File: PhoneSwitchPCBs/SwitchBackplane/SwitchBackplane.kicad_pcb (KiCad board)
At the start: 2 copper layers, 255 parts, among them J1 Power, J10 Trunk 1, J11 Trunk 2, J12 UART, J13 SWD, J2 Station 1, J3 Station 2, J4 Station 3, J5 Station 4, J6 Station 5, J7 Station 6, J8 Station 7, J9 Station 8, Q1 XP231N02013R-G, Q10 XP231N02013R-G, Q11 XP231N02013R-G, Q12 PMV65XP, Q2 XP231N02013R-G, Q3 XP231N02013R-G, Q4 XP231N02013R-G, Q5 XP231N02013R-G, Q6 XP231N02013R-G, Q7 XP231N02013R-G, Q8 XP231N02013R-G, Q9 XP231N02013R-G, T1 FS28-200-C2, U1 Pi Pico, U10 XRA1403IG24TR-F, U11 TL071, U12 TL071, U13 XRA1403IG24TR-F, U14 XRA1403IG24TR-F, U15 XRA1403IG24TR-F, U2 TL074, U3 TL074, U4 74HC4316, U5 TL071, U6 MT8870DS1, U7 TPA3144D2PWPR, U8 MT8870DS1, U9 74HC4316, Y1 3.579545 MHz

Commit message: More work on PCB
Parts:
- added H1: GND, MountingHole:MountingHole_3.2mm_M3_Pad, F.Cu at (53.5, 60.8)
- added H2: GND, MountingHole:MountingHole_3.2mm_M3_Pad, F.Cu at (53.5, 155.1)
- added H3: GND, MountingHole:MountingHole_3.2mm_M3_Pad, F.Cu at (221.2, 60.8)
- added H4: GND, MountingHole:MountingHole_3.2mm_M3_Pad, F.Cu at (221.2, 155.1)
- added H5: GND, MountingHole:MountingHole_3.2mm_M3_Pad, F.Cu at (389.0, 60.8)
- added H6: GND, MountingHole:MountingHole_3.2mm_M3_Pad, F.Cu at (389.0, 155.1)
- moved C3 139.3 mm to (266.8, 227.1)
- moved C38 139.3 mm to (190.7, 256.9)
- moved Q7 139.3 mm to (210.1, 256.9)
- moved R52 139.3 mm to (266.8, 229.6)
- moved R91 139.3 mm to (266.8, 224.6)
- moved U3 139.3 mm to (264.8, 179.9)
- moved C1 139.3 mm to (145.2, 260.1)
- moved C10 139.3 mm to (233.4, 234.7)
- moved C11 139.3 mm to (266.7, 232.1)
- moved C12 139.3 mm to (281.5, 215.8)
- moved C13 139.3 mm to (262.0, 236.6)
- moved C14 139.3 mm to (242.9, 254.0)
- moved C15 139.3 mm to (266.2, 202.9)
- moved C16 139.3 mm to (256.9, 241.4)
- moved C17 139.3 mm to (279.7, 212.9)
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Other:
- board outline added: 342.9 x 101.6 mm

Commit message: Adjusted PCB Dimensions
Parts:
- moved T1 229.6 mm to (365.7, 78.0), turned to 270 degrees
- moved U7 141.5 mm to (365.8, 112.3)
- moved H2 39.1 mm to (36.1, 120.0)
- moved H4 36.8 mm to (210.2, 120.0)
- moved H6 35.4 mm to (384.3, 120.0)
- moved H1 19.9 mm to (36.1, 51.2)
- moved H3 14.7 mm to (210.2, 51.2)
- moved H5 10.7 mm to (384.3, 51.2)
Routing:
- added copper zone on B.Cu, net GND
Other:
- board size 342.9 x 101.6 mm -> 355.6 x 76.2 mm

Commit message: Align module connectors
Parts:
- U7: moved to B.Cu
- moved J10 198.2 mm to (329.6, 79.9), turned to 270 degrees
- moved J6 168.9 mm to (222.9, 79.9), turned to 270 degrees
- moved J11 167.3 mm to (304.2, 91.3), turned to 90 degrees
- moved U1 162.0 mm to (54.6, 73.5)
- moved J3 153.2 mm to (90.8, 91.3), turned to 90 degrees
- moved J2 146.7 mm to (116.2, 79.9), turned to 270 degrees
- moved J9 144.2 mm to (250.8, 91.3), turned to 90 degrees
- moved J5 140.5 mm to (144.1, 91.3), turned to 90 degrees
- moved J4 107.8 mm to (169.5, 79.9), turned to 270 degrees
- moved J8 107.5 mm to (276.2, 79.9), turned to 270 degrees
- moved J7 89.6 mm to (197.5, 91.3), turned to 90 degrees
- moved U7 26.7 mm to (365.8, 85.6)
- moved T1 7.65 mm to (365.6, 85.6)

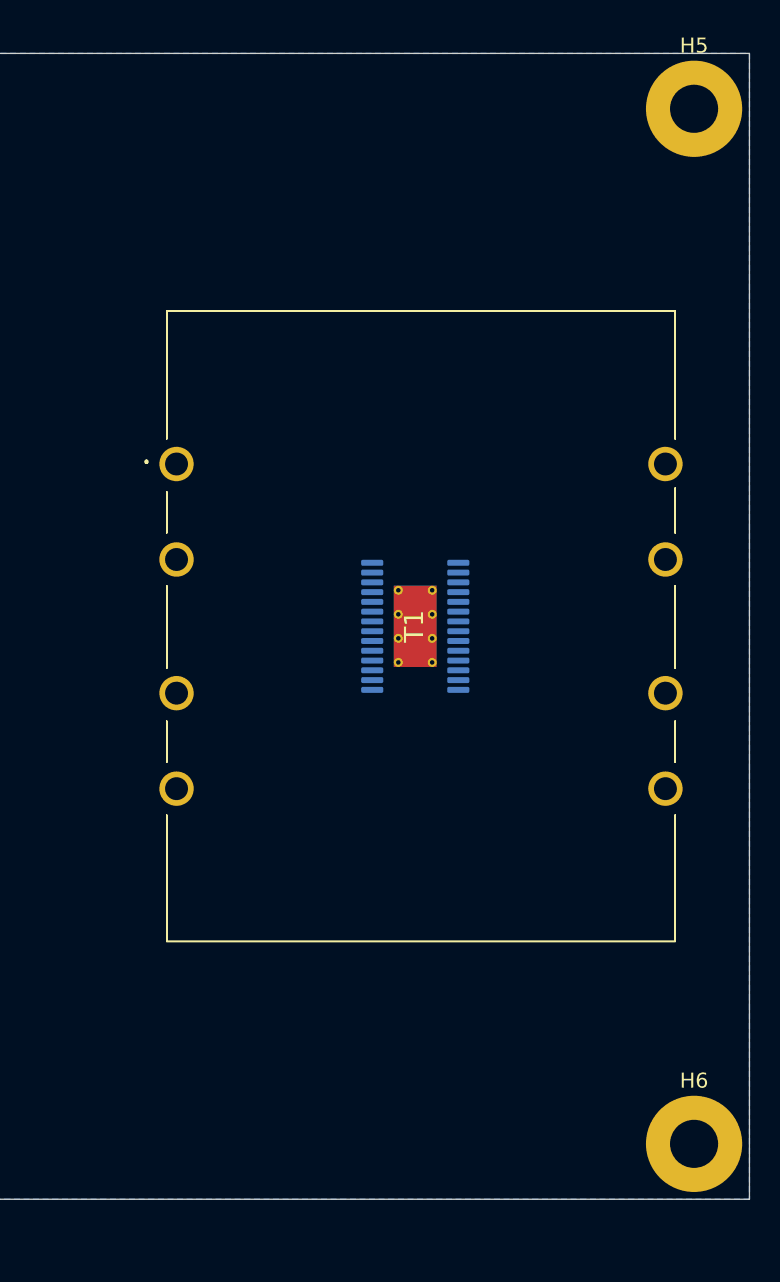
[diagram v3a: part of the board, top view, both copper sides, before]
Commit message: Added more mounting holes for transformer
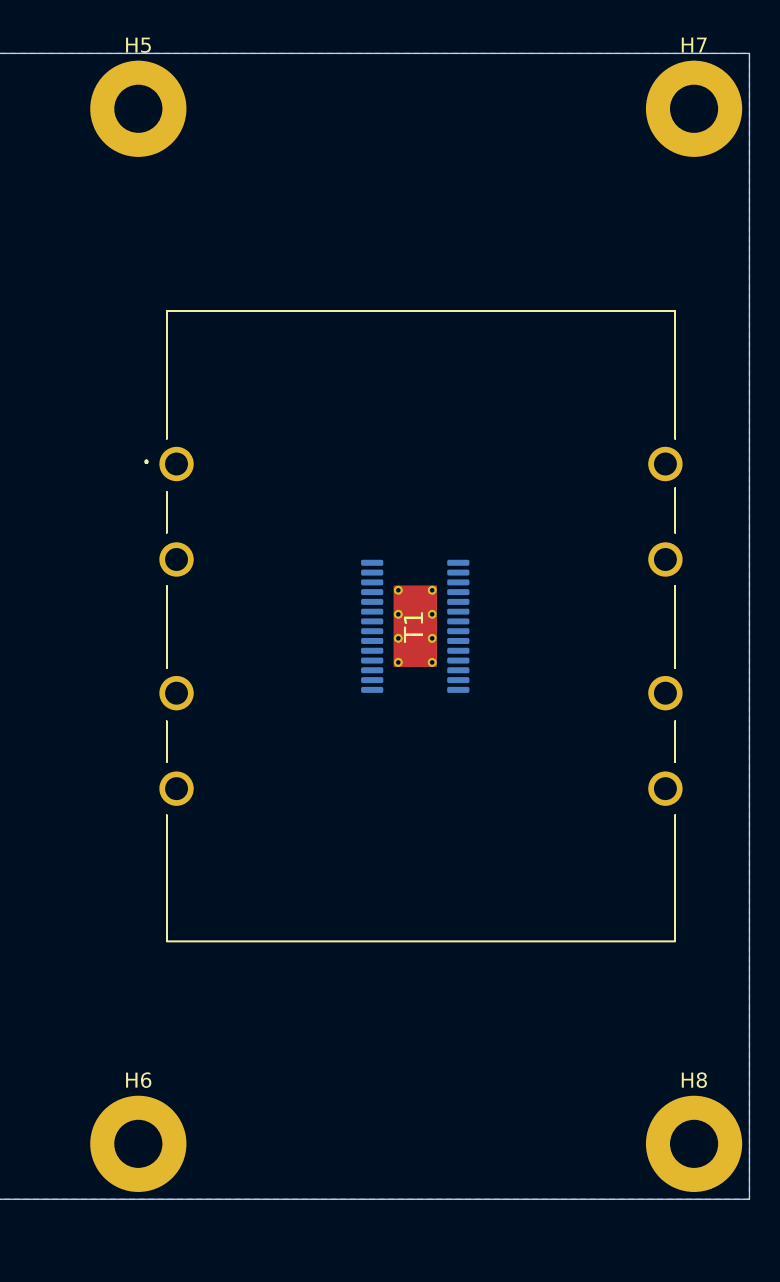
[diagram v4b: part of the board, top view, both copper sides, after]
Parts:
- added H7: GND, MountingHole:MountingHole_3.2mm_M3_Pad, F.Cu at (384.3, 51.2)
- added H8: GND, MountingHole:MountingHole_3.2mm_M3_Pad, F.Cu at (384.3, 120.0)
- moved H5 37.0 mm to (347.3, 51.2)
- moved H6 37.0 mm to (347.3, 120.0)

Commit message: more PCB chaos
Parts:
- C27, C31, C34, C43, C44, C50, C51, FB1, FB2, R20, R25: moved to B.Cu
- moved C44 243.1 mm to (372.7, 81.4), turned to 180 degrees
- moved C50 230.8 mm to (379.6, 71.4), turned to 270 degrees
- moved FB1 213.9 mm to (378.8, 74.8)
- moved C43 209.7 mm to (367.1, 103.6)
- moved J1 203.4 mm to (38.0, 93.5), turned to 90 degrees
- moved F2 195.2 mm to (58.5, 120.9), turned to 90 degrees
- moved F1 192.9 mm to (47.0, 120.9), turned to 90 degrees
- moved C51 144.1 mm to (379.6, 99.8), turned to 270 degrees
- moved FB2 144.0 mm to (378.8, 96.4)
- moved R25 134.3 mm to (349.4, 202.8)
- moved F3 129.8 mm to (357.8, 111.3), turned to 270 degrees
- moved C34 124.7 mm to (349.1, 194.3)
- moved C31 122.0 mm to (347.1, 179.5)
- moved R20 119.2 mm to (361.5, 201.4)
- moved C27 57.1 mm to (335.2, 190.6)
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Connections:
- FB1 pad 1: Net-(C43-Pad1) -> Net-(C44-Pad1)
- FB2 pad 1: Net-(C44-Pad1) -> Net-(C43-Pad1)
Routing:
- net GND: track 0.00 -> 24.7 mm
- net Net-(C44-Pad1): track 0.00 -> 20.7 mm
- net Net-(C43-Pad1): track 0.00 -> 20.3 mm
- net Net-(T1-Pad6): track 0.00 -> 8.89 mm
- net Net-(T1-Pad2): track 0.00 -> 8.89 mm
- net Net-(C51-Pad1): track 0.00 -> 5.36 mm
- net Net-(C50-Pad2): track 0.00 -> 5.34 mm
- net +12V: track 0.00 -> 1.30 mm
- net Net-(Q3-Pad3): track 0.00 -> 0.65 mm
- added copper zone on F.Cu, net GND

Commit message: Connect voice and tone pins
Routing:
- net /T2R: track 0.00 -> 511.8 mm, vias 0 -> 12
- net /T1T: track 0.00 -> 511.8 mm, vias 0 -> 12
- net /T1R: track 0.00 -> 511.8 mm, vias 0 -> 12
- net /T2T: track 0.00 -> 511.8 mm, vias 0 -> 12
- net /V1T: track 0.00 -> 295.9 mm, vias 0 -> 10
- net /V1R: track 0.00 -> 290.8 mm, vias 0 -> 10
- net /V2T: track 0.00 -> 285.8 mm, vias 0 -> 10
- net /V2R: track 0.00 -> 280.7 mm, vias 0 -> 10

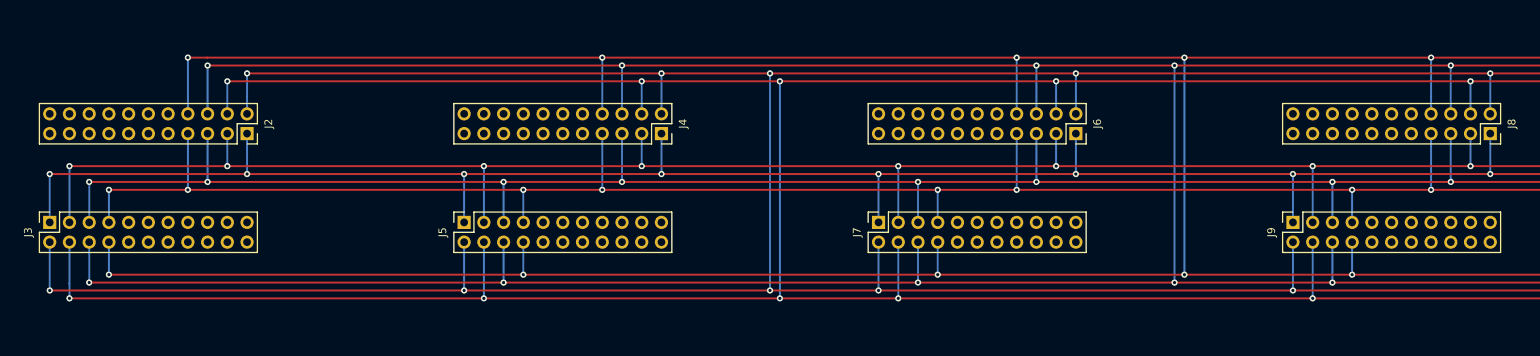
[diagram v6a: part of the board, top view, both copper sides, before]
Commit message: More track routing
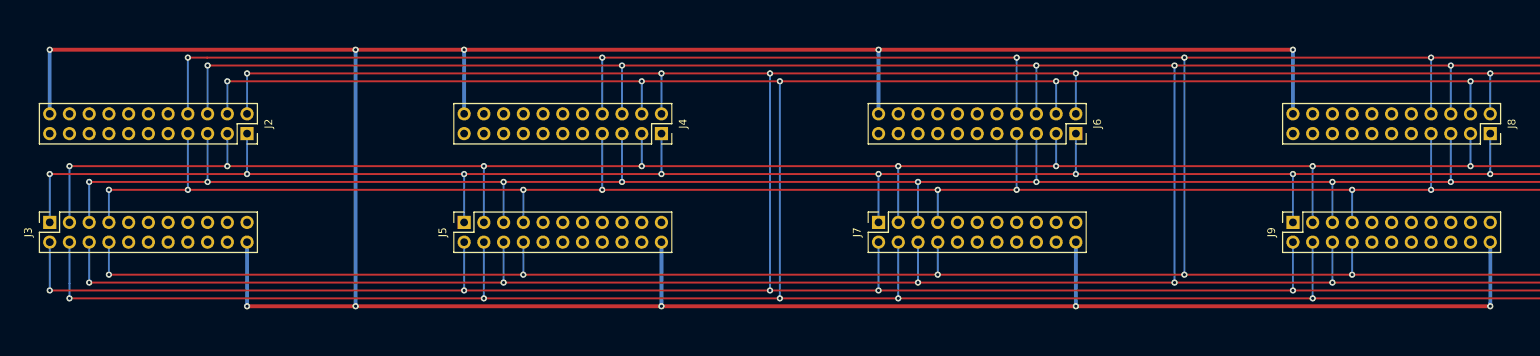
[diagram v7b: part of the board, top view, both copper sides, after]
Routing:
- net -48V: track 0.00 -> 419.1 mm, vias 0 -> 10
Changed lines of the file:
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@@
     (thickness 1.6)
     (drawings 24)
-    (tracks 303)
+    (tracks 331)
     (zones 0)
     (modules 263)
@@
   )
   (setup
-    (last_trace_width 0.25)
+    (last_trace_width 0.499872)
     (user_trace_width 0.499872)
     (user_trace_width 0.749808)
@@
   (segment (start 271.145 71.12) (end 235.585 71.12) (width 0.25) (layer F.Cu) (net 45))
   (segment (start 324.485 71.12) (end 271.145 71.12) (width 0.25) (layer F.Cu) (net 45))
+  (segment (start 276.225 101.766064) (end 276.225 93.853) (width 0.499872) (layer B.Cu) (net 47))
+  (segment (start 276.225 102.108) (end 276.225 101.766064) (width 0.499872) (layer B.Cu) (net 47))
+  (via (at 276.225 102.108) (size 0.8) (drill 0.4) (layers F.Cu B.Cu) (net 47))
+  (via (at 116.205 102.108) (size 0.8) (drill 0.4) (layers F.Cu B.Cu) (net 47))
+  (segment (start 116.205 102.108) (end 116.205 93.853) (width 0.499872) (layer B.Cu) (net 47))
+  (via (at 169.545 102.108) (size 0.8) (drill 0.4) (layers F.Cu B.Cu) (net 47))
+  (segment (start 169.545 93.853) (end 169.545 102.108) (width 0.499872) (layer B.Cu) (net 47))
+  (via (at 222.885 102.108) (size 0.8) (drill 0.4) (layers F.Cu B.Cu) (net 47))
+  (segment (start 222.885 93.853) (end 222.885 102.108) (width 0.499872) (layer B.Cu) (net 47))
+  (segment (start 222.885 102.108) (end 169.545 102.108) (width 0.499872) (layer F.Cu) (net 47))
+  (segment (start 276.225 102.108) (end 222.885 102.108) (width 0.499872) (layer F.Cu) (net 47))
+  (segment (start 90.805 77.343) (end 90.805 69.088) (width 0.499872) (layer B.Cu) (net 47))
+  (via (at 90.805 69.088) (size 0.8) (drill 0.4) (layers F.Cu B.Cu) (net 47))
+  (via (at 250.825 69.088) (size 0.8) (drill 0.4) (layers F.Cu B.Cu) (net 47))
+  (segment (start 250.825 69.088) (end 250.825 77.343) (width 0.499872) (layer B.Cu) (net 47))
+  (via (at 197.485 69.088) (size 0.8) (drill 0.4) (layers F.Cu B.Cu) (net 47))
+  (segment (start 197.485 77.343) (end 197.485 69.088) (width 0.499872) (layer B.Cu) (net 47))
+  (segment (start 197.485 69.088) (end 250.825 69.088) (width 0.499872) (layer F.Cu) (net 47))
+  (via (at 144.145 69.088) (size 0.8) (drill 0.4) (layers F.Cu B.Cu) (net 47))
+  (segment (start 144.145 77.343) (end 144.145 69.088) (width 0.499872) (layer B.Cu) (net 47))
+  (segment (start 144.145 69.088) (end 197.485 69.088) (width 0.499872) (layer F.Cu) (net 47))
+  (via (at 130.175 69.088) (size 0.8) (drill 0.4) (layers F.Cu B.Cu) (net 47))
+  (segment (start 90.805 69.088) (end 130.175 69.088) (width 0.499872) (layer F.Cu) (net 47))
+  (segment (start 130.175 69.088) (end 144.145 69.088) (width 0.499872) (layer F.Cu) (net 47))
+  (via (at 130.175 102.108) (size 0.8) (drill 0.4) (layers F.Cu B.Cu) (net 47))
+  (segment (start 130.175 102.108) (end 116.205 102.108) (width 0.499872) (layer F.Cu) (net 47))
+  (segment (start 130.175 69.088) (end 130.175 102.108) (width 0.499872) (layer B.Cu) (net 47))
+  (segment (start 169.545 102.108) (end 130.175 102.108) (width 0.499872) (layer F.Cu) (net 47))
   (segment (start 321.945 88.646002) (end 321.945 88.646) (width 0.25) (layer F.Cu) (net 100))
   (via (at 321.945 87.122) (size 0.8) (drill 0.4) (layers F.Cu B.Cu) (net 100))
